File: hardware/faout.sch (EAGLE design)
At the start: 159 parts, among them IC2 MT48LC8M16A2, P1 TE_CONN_MTE_HEADER3R, Q1 L7812ACV, Q2 L7912ACV, Q3 12MHz, Q4 ASFL, U1 LM3671MF-3.3, U10 REF102AU, U11 OPA4277UA, U12 DAC8812, U13 REF102AU, U14 OPA4277UA, U15 DAC8812, U2 LM3671MF-1.2, U3 93LC46BT-I/OT, U4 6SLX9TQG144, U5 M25PE16SO8N, U6 OPA2277UA/2K5E4, U7 REF102AU, U8 OPA4277UA, U9 DAC8812

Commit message: Order code corrections and additions.
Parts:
- C17, C9: OC_FARNELL 9693467 -> 317287
- R18, R19, R22, R23, R24, R25, R28, R29, R30, R31, R34, R35: OC_FARNELL (none) -> 1688472

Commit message: Update UCF file for new board layout.
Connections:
- removed net P1_8: SV2.8, U4B1.IO_L32N_1
- new net P1_0: SV2.1, U4B1.IO_L42P_GCLK7_1
- net P1_1: now also SV2.2, U4B1.IO_L42N_GCLK6_TRDY1_1; no longer SV2.1, U4B1.IO_L42P_GCLK7_1
- net P1_2: now also SV2.3, U4B1.IO_L41P_GCLK9_IRDY1_1; no longer SV2.2, U4B1.IO_L42N_GCLK6_TRDY1_1
- net P1_3: now also SV2.4, U4B1.IO_L41N_GCLK8_1; no longer SV2.3, U4B1.IO_L41P_GCLK9_IRDY1_1
- net P1_4: now also SV2.5, U4B1.IO_L33P_1; no longer SV2.4, U4B1.IO_L41N_GCLK8_1
- net P1_5: now also SV2.6, U4B1.IO_L33N_1; no longer SV2.5, U4B1.IO_L33P_1
- net P1_6: now also SV2.7, U4B1.IO_L32P_1; no longer SV2.6, U4B1.IO_L33N_1
- net P1_7: now also SV2.8, U4B1.IO_L32N_1; no longer SV2.7, U4B1.IO_L32P_1
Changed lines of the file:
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@@
 </segment>
 <segment>
-<wire x1="248.92" y1="-116.84" x2="236.22" y2="-116.84" width="0.1524" layer="91"/>
+<wire x1="248.92" y1="-116.84" x2="233.68" y2="-116.84" width="0.1524" layer="91"/>
 <label x="236.22" y="-116.84" size="1.778" layer="95"/>
 <pinref part="U4" gate="B0" pin="IO_L3P_0"/>
-<junction x="236.22" y="-116.84"/>
-<wire x1="236.22" y1="-116.84" x2="233.68" y2="-116.84" width="0.1524" layer="91"/>
 </segment>
 </net>
@@
 </segment>
 <segment>
-<wire x1="248.92" y1="-124.46" x2="236.22" y2="-124.46" width="0.1524" layer="91"/>
+<wire x1="248.92" y1="-124.46" x2="233.68" y2="-124.46" width="0.1524" layer="91"/>
 <label x="236.22" y="-124.46" size="1.778" layer="95"/>
 <pinref part="U4" gate="B0" pin="IO_L2N_0"/>
-<junction x="236.22" y="-124.46"/>
-<wire x1="236.22" y1="-124.46" x2="233.68" y2="-124.46" width="0.1524" layer="91"/>
 </segment>
 </net>
@@
 </segment>
 </net>
+<net name="P1_0" class="0">
+<segment>
+<pinref part="U4" gate="B1" pin="IO_L42P_GCLK7_1"/>
+<wire x1="233.68" y1="-198.12" x2="248.92" y2="-198.12" width="0.1524" layer="91"/>
+<label x="236.22" y="-198.12" size="1.778" layer="95"/>
+</segment>
+<segment>
+<wire x1="10.16" y1="-279.4" x2="22.86" y2="-279.4" width="0.1524" layer="91"/>
+<label x="12.7" y="-279.4" size="1.778" layer="95"/>
+<pinref part="SV2" gate="G$1" pin="1"/>
+</segment>
+</net>
+<net name="P1_3" class="0">
+<segment>
+<pinref part="U4" gate="B1" pin="IO_L41N_GCLK8_1"/>
+<wire x1="233.68" y1="-190.5" x2="248.92" y2="-190.5" width="0.1524" layer="91"/>
+<label x="236.22" y="-190.5" size="1.778" layer="95"/>
+</segment>
+<segment>
+<wire x1="-17.78" y1="-276.86" x2="-5.08" y2="-276.86" width="0.1524" layer="91"/>
+<label x="-15.24" y="-276.86" size="1.778" layer="95"/>
+<pinref part="SV2" gate="G$1" pin="4"/>
+</segment>
+</net>
 <net name="P1_2" class="0">
+<segment>
+<pinref part="U4" gate="B1" pin="IO_L41P_GCLK9_IRDY1_1"/>
+<wire x1="233.68" y1="-193.04" x2="248.92" y2="-193.04" width="0.1524" layer="91"/>
+<label x="236.22" y="-193.04" size="1.778" layer="95"/>
+</segment>
+<segment>
+<wire x1="10.16" y1="-276.86" x2="22.86" y2="-276.86" width="0.1524" layer="91"/>
+<label x="12.7" y="-276.86" size="1.778" layer="95"/>
+<pinref part="SV2" gate="G$1" pin="3"/>
+</segment>
+</net>
+<net name="P1_6" class="0">
+<segment>
+<pinref part="U4" gate="B1" pin="IO_L32P_1"/>
+<wire x1="233.68" y1="-172.72" x2="248.92" y2="-172.72" width="0.1524" layer="91"/>
+<label x="236.22" y="-172.72" size="1.778" layer="95"/>
+</segment>
+<segment>
+<wire x1="10.16" y1="-271.78" x2="22.86" y2="-271.78" width="0.1524" layer="91"/>
+<label x="12.7" y="-271.78" size="1.778" layer="95"/>
+<pinref part="SV2" gate="G$1" pin="7"/>
+</segment>
+</net>
+<net name="P1_7" class="0">
+<segment>
+<pinref part="U4" gate="B1" pin="IO_L32N_1"/>
+<wire x1="233.68" y1="-170.18" x2="248.92" y2="-170.18" width="0.1524" layer="91"/>
+<label x="236.22" y="-170.18" size="1.778" layer="95"/>
+</segment>
+<segment>
+<wire x1="-17.78" y1="-271.78" x2="-5.08" y2="-271.78" width="0.1524" layer="91"/>
+<label x="-15.24" y="-271.78" size="1.778" layer="95"/>
+<pinref part="SV2" gate="G$1" pin="8"/>
+</segment>
+</net>
+<net name="P1_4" class="0">
+<segment>
+<pinref part="U4" gate="B1" pin="IO_L33P_1"/>
+<wire x1="248.92" y1="-177.8" x2="233.68" y2="-177.8" width="0.1524" layer="91"/>
+<label x="236.22" y="-177.8" size="1.778" layer="95"/>
+</segment>
+<segment>
+<wire x1="22.86" y1="-274.32" x2="10.16" y2="-274.32" width="0.1524" layer="91"/>
+<label x="12.7" y="-274.32" size="1.778" layer="95"/>
+<pinref part="SV2" gate="G$1" pin="5"/>
+</segment>
+</net>
+<net name="P1_5" class="0">
+<segment>
+<pinref part="U4" gate="B1" pin="IO_L33N_1"/>
+<wire x1="233.68" y1="-175.26" x2="248.92" y2="-175.26" width="0.1524" layer="91"/>
+<label x="236.22" y="-175.26" size="1.778" layer="95"/>
+</segment>
+<segment>
+<wire x1="-17.78" y1="-274.32" x2="-5.08" y2="-274.32" width="0.1524" layer="91"/>
+<label x="-15.24" y="-274.32" size="1.778" layer="95"/>
+<pinref part="SV2" gate="G$1" pin="6"/>
+</segment>
+</net>
+<net name="P1_1" class="0">
+<segment>
+<wire x1="-17.78" y1="-279.4" x2="-5.08" y2="-279.4" width="0.1524" layer="91"/>
+<label x="-15.24" y="-279.4" size="1.778" layer="95"/>
+<pinref part="SV2" gate="G$1" pin="2"/>
+</segment>
 <segment>
 <pinref part="U4" gate="B1" pin="IO_L42N_GCLK6_TRDY1_1"/>
@@
 <label x="236.22" y="-195.58" size="1.778" layer="95"/>
 </segment>
-<segment>
-<wire x1="-17.78" y1="-279.4" x2="-5.08" y2="-279.4" width="0.1524" layer="91"/>
-<label x="-15.24" y="-279.4" size="1.778" layer="95"/>
-<pinref part="SV2" gate="G$1" pin="2"/>
-</segment>
-</net>
-<net name="P1_1" class="0">
-<segment>
-<pinref part="U4" gate="B1" pin="IO_L42P_GCLK7_1"/>
-<wire x1="233.68" y1="-198.12" x2="248.92" y2="-198.12" width="0.1524" layer="91"/>
-<label x="236.22" y="-198.12" size="1.778" layer="95"/>
-</segment>
-<segment>
-<wire x1="10.16" y1="-279.4" x2="22.86" y2="-279.4" width="0.1524" layer="91"/>
-<label x="12.7" y="-279.4" size="1.778" layer="95"/>
-<pinref part="SV2" gate="G$1" pin="1"/>
-</segment>
-</net>
-<net name="P1_4" class="0">
-<segment>
-<pinref part="U4" gate="B1" pin="IO_L41N_GCLK8_1"/>
-<wire x1="233.68" y1="-190.5" x2="248.92" y2="-190.5" width="0.1524" layer="91"/>
-<label x="236.22" y="-190.5" size="1.778" layer="95"/>
-</segment>
-<segment>
-<wire x1="-17.78" y1="-276.86" x2="-5.08" y2="-276.86" width="0.1524" layer="91"/>
-<label x="-15.24" y="-276.86" size="1.778" layer="95"/>
-<pinref part="SV2" gate="G$1" pin="4"/>
-</segment>
-</net>
-<net name="P1_3" class="0">
-<segment>
-<pinref part="U4" gate="B1" pin="IO_L41P_GCLK9_IRDY1_1"/>
-<wire x1="233.68" y1="-193.04" x2="248.92" y2="-193.04" width="0.1524" layer="91"/>
-<label x="236.22" y="-193.04" size="1.778" layer="95"/>
-</segment>
-<segment>
-<wire x1="10.16" y1="-276.86" x2="22.86" y2="-276.86" width="0.1524" layer="91"/>
-<label x="12.7" y="-276.86" size="1.778" layer="95"/>
-<pinref part="SV2" gate="G$1" pin="3"/>
-</segment>
-</net>
-<net name="P1_7" class="0">
-<segment>
-<pinref part="U4" gate="B1" pin="IO_L32P_1"/>
-<wire x1="233.68" y1="-172.72" x2="248.92" y2="-172.72" width="0.1524" layer="91"/>
-<label x="236.22" y="-172.72" size="1.778" layer="95"/>
-</segment>
-<segment>
-<wire x1="10.16" y1="-271.78" x2="22.86" y2="-271.78" width="0.1524" layer="91"/>
-<label x="12.7" y="-271.78" size="1.778" layer="95"/>
-<pinref part="SV2" gate="G$1" pin="7"/>
-</segment>
-</net>
-<net name="P1_8" class="0">
-<segment>
-<pinref part="U4" gate="B1" pin="IO_L32N_1"/>
-<wire x1="233.68" y1="-170.18" x2="248.92" y2="-170.18" width="0.1524" layer="91"/>
-<label x="236.22" y="-170.18" size="1.778" layer="95"/>
-</segment>
-<segment>
-<wire x1="-17.78" y1="-271.78" x2="-5.08" y2="-271.78" width="0.1524" layer="91"/>
-<label x="-15.24" y="-271.78" size="1.778" layer="95"/>
-<pinref part="SV2" gate="G$1" pin="8"/>
-</segment>
-</net>
-<net name="P1_5" class="0">
-<segment>
-<pinref part="U4" gate="B1" pin="IO_L33P_1"/>
-<wire x1="248.92" y1="-177.8" x2="233.68" y2="-177.8" width="0.1524" layer="91"/>
-<label x="236.22" y="-177.8" size="1.778" layer="95"/>
-</segment>
-<segment>
-<wire x1="22.86" y1="-274.32" x2="10.16" y2="-274.32" width="0.1524" layer="91"/>
-<label x="12.7" y="-274.32" size="1.778" layer="95"/>
-<pinref part="SV2" gate="G$1" pin="5"/>
-</segment>
-</net>
-<net name="P1_6" class="0">
-<segment>
-<pinref part="U4" gate="B1" pin="IO_L33N_1"/>
-<wire x1="233.68" y1="-175.26" x2="248.92" y2="-175.26" width="0.1524" layer="91"/>
-<label x="236.22" y="-175.26" size="1.778" layer="95"/>
-</segment>
-<segment>
-<wire x1="-17.78" y1="-274.32" x2="-5.08" y2="-274.32" width="0.1524" layer="91"/>
-<label x="-15.24" y="-274.32" size="1.778" layer="95"/>
-<pinref part="SV2" gate="G$1" pin="6"/>
-</segment>
-</net>
+</net>

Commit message: Rework DAC power supply. Precision resistor arrays for outputs.
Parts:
- removed R18, R19, R22, R23, R24, R25, R28, R29, R30, R31, R34, R35: 10k, faout:R_EU0603
- removed R20, R21, R26, R27, R32, R33: 5k, faout:R_EU0603
- removed U6: OPA2277UA/2K5E4, faout:OPA2277UA/2K5E4
- added C100, C101, C102, C103, C98, C99: 10uF, faout:C_EU0805
- added C92, C93, C94, C97: 1uF, faout:C_EU0603
- added C95: 220uF, rcl:CPOL-EUE
- added C96: 10nF, faout:C_EU0603
- added RN1, RN2, RN3, RN4, RN5, RN6: 10k, resistor-dil:4R-NEXBV8V
- added U16: LM7321MF, faout:LM7321MF
- C17, C9: value 100uF -> 220uF; OC_FARNELL 317287 -> 9695680
- C73, C82, C91: value 100nF -> 10nF; OC_FARNELL 1740621 -> 1759102
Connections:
- removed net N$20: R27.P$2, R28.P$1, R29.P$2, U11.-IN_C
- removed net N$21: R24.P$1, R25.P$2, R26.P$2, U11.-IN_D
- new net N$16: RN1A.2, RN1B.2, RN1C.2, RN1D.1, U8.-IN_D
- new net N$17: RN3A.2, RN3B.2, RN3C.2, RN3D.1, U11.-IN_D
- net A+12V: now also C100.P$1, C102.P$1, C96.P$1, C97.P$1, C98.P$1, U16.V+; no longer U6.V+
- net A+3V3: now also C92.P$1, C93.P$1, C94.P$1, C95.+, U16.-IN, U16.OUT; no longer U6.-IN_A, U6.OUT_A
- net A-12V: now also C101.P$2, C103.P$2, C99.P$2
- net AGND: now also C100.P$2, C101.P$1, C102.P$2, C103.P$1, C92.P$2, C93.P$2, C94.P$2, C95.-, C96.P$2, C97.P$2, C98.P$2, C99.P$1, U16.V-; no longer U6.V-
- net DAC1_RFBA: now also RN2B.2, RN2C.2; no longer R21.P$1
- net DAC1_RFBB: now also RN1B.1, RN1C.1; no longer R20.P$1
- net DAC1_VOUTA: now also RN2D.1; no longer R23.P$1
- net DAC1_VOUTB: now also RN1D.2; no longer R19.P$1
- net DAC1_VREF: now also RN1A.1, RN2A.2; no longer R18.P$2, R22.P$2
- net DAC2_RFBA: now also RN4B.2, RN4C.2; no longer R27.P$1
- net DAC2_RFBB: now also RN3B.1, RN3C.1; no longer R26.P$1
- net DAC2_VOUTA: now also RN4D.1; no longer R29.P$1
- net DAC2_VOUTB: now also RN3D.2; no longer R25.P$1
- net DAC2_VREF: now also RN3A.1, RN4A.2; no longer R24.P$2, R28.P$2
- net DAC3_RFBA: now also RN6B.2, RN6C.2; no longer R33.P$1
- net DAC3_RFBB: now also RN5B.1, RN5C.1; no longer R32.P$1
- net DAC3_VOUTA: now also RN6D.1; no longer R35.P$1
- net DAC3_VOUTB: now also RN5D.2; no longer R31.P$1
- net DAC3_VREF: now also RN5A.1, RN6A.2; no longer R30.P$2, R34.P$2
- net N$10: now also RN5A.2, RN5B.2, RN5C.2, RN5D.1; no longer R30.P$1, R31.P$2, R32.P$2
- net N$13: now also U16.+IN; no longer U6.+IN_A
- net N$14: now also RN6A.1, RN6B.1, RN6C.1, RN6D.2; no longer R33.P$2, R34.P$1, R35.P$2
- net N$8: now also RN2A.1, RN2B.1, RN2C.1, RN2D.2; no longer R21.P$2, R22.P$1, R23.P$2
- net N$9: now also RN4A.1, RN4B.1, RN4C.1, RN4D.2, U11.-IN_C; no longer R18.P$1, R19.P$2, R20.P$2, U8.-IN_D
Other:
- moved on the sheet: C73, C82, C91, R16, R17

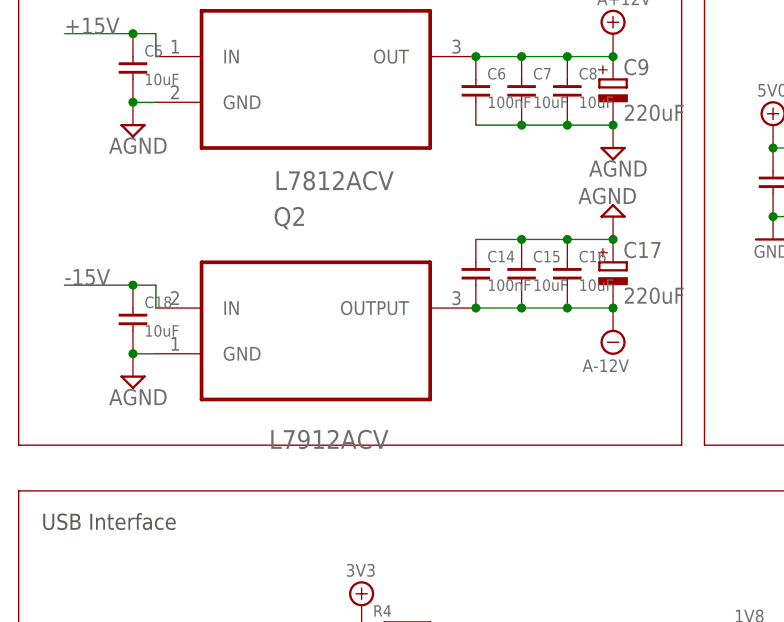
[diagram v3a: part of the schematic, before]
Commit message: Analog power supply with low profile components.
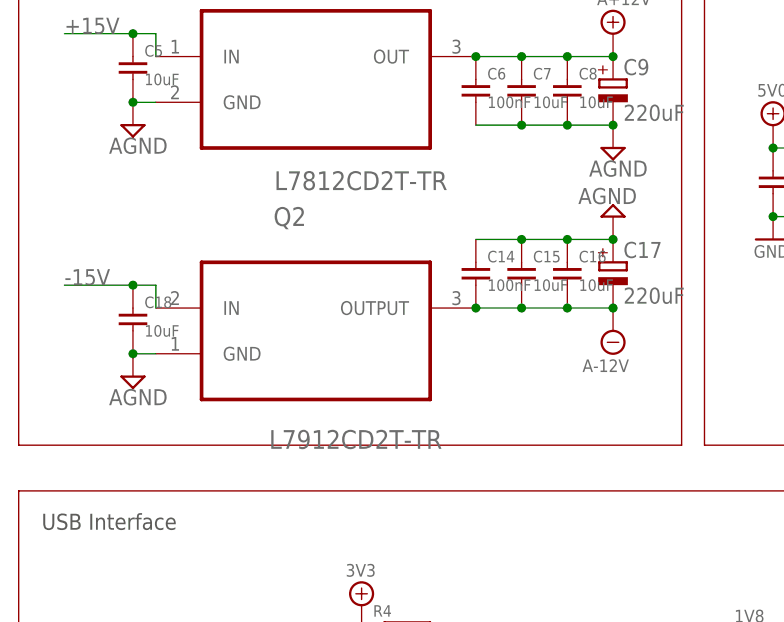
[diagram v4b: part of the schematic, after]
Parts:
- Q1: value L7812ACV -> L7812CD2T-TR; device faout:L7812ACV -> faout:L7812CD2T-TR
- Q2: value L7912ACV -> L7912CD2T-TR; device faout:L7912ACV -> faout:L7912CD2T-TR
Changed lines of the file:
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@@
 <attribute name="OC_FARNELL" value="1833803"/>
 </part>
-<part name="Q1" library="faout" deviceset="L7812ACV" device=""/>
-<part name="Q2" library="faout" deviceset="L7912ACV" device=""/>
+<part name="Q1" library="faout" deviceset="L7812CD2T-TR" device=""/>
+<part name="Q2" library="faout" deviceset="L7912CD2T-TR" device=""/>
 <part name="A+12V_PWR1" library="faout" deviceset="A+12V" device=""/>
 <part name="A-12V_PWR1" library="faout" deviceset="A-12V" device=""/>

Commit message: Add and correct Farnell order codes.
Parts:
- Q1: OC_FARNELL (none) -> 2296017
- R1, R3: OC_FARNELL (none) -> 1612060
- R4, R5: OC_FARNELL (none) -> 1463451
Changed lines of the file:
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@@
 <part name="GND_PWR10" library="faout" deviceset="GND" device=""/>
 <part name="GND_PWR9" library="faout" deviceset="GND" device=""/>
-<part name="R4" library="faout" deviceset="R_EU" device="0603" value="ferrite"/>
-<part name="R5" library="faout" deviceset="R_EU" device="0603" value="ferrite"/>
+<part name="R4" library="faout" deviceset="R_EU" device="0603" value="ferrite">
+<attribute name="OC_FARNELL" value="1463451"/>
+</part>
+<part name="R5" library="faout" deviceset="R_EU" device="0603" value="ferrite">
+<attribute name="OC_FARNELL" value="1463451"/>
+</part>
 <part name="C19" library="faout" deviceset="C_EU" device="0603" value="4.7uF">
 <attribute name="OC_FARNELL" value="1833803"/>
@@
 <attribute name="OC_FARNELL" value="1833803"/>
 </part>
-<part name="Q1" library="faout" deviceset="L7812CD2T-TR" device=""/>
+<part name="Q1" library="faout" deviceset="L7812CD2T-TR" device="">
+<attribute name="OC_FARNELL" value="2296017"/>
+</part>
 <part name="Q2" library="faout" deviceset="L7912CD2T-TR" device=""/>
 <part name="A+12V_PWR1" library="faout" deviceset="A+12V" device=""/>
@@
 <part name="GND_PWR21" library="faout" deviceset="GND" device=""/>
 <part name="R7" library="faout" deviceset="R_EU" device="0603" value="NC"/>
-<part name="R1" library="faout" deviceset="R_EU" device="1206" value="ferrite"/>
-<part name="R3" library="faout" deviceset="R_EU" device="1206" value="ferrite"/>
+<part name="R1" library="faout" deviceset="R_EU" device="1206" value="ferrite">
+<attribute name="OC_FARNELL" value="1612060"/>
+</part>
+<part name="R3" library="faout" deviceset="R_EU" device="1206" value="ferrite">
+<attribute name="OC_FARNELL" value="1612060"/>
+</part>
 <part name="5V0_PWR1" library="Bogdan_Commons" deviceset="5V0" device=""/>
 <part name="GND_PWR2" library="Bogdan_Commons" deviceset="GND" device=""/>
@@
 <instance part="GND_PWR10" gate="A" x="45.72" y="-60.96"/>
 <instance part="GND_PWR9" gate="A" x="40.64" y="-60.96"/>
-<instance part="R4" gate="G$1" x="20.32" y="-45.72"/>
-<instance part="R5" gate="G$1" x="20.32" y="-48.26"/>
+<instance part="R4" gate="G$1" x="20.32" y="-45.72">
+<attribute name="OC_FARNELL" x="20.32" y="-45.72" size="1.778" layer="96" display="off"/>
+</instance>
+<instance part="R5" gate="G$1" x="20.32" y="-48.26">
+<attribute name="OC_FARNELL" x="20.32" y="-48.26" size="1.778" layer="96" display="off"/>
+</instance>
 <instance part="C19" gate="G$1" x="27.94" y="-53.34">
 <attribute name="OC_FARNELL" x="27.94" y="-53.34" size="1.778" layer="96" display="off"/>
@@
 <instance part="GND_PWR21" gate="A" x="-5.08" y="-236.22" rot="R180"/>
 <instance part="R7" gate="G$1" x="53.34" y="-142.24" rot="R270"/>
-<instance part="R1" gate="G$1" x="116.84" y="63.5"/>
-<instance part="R3" gate="G$1" x="116.84" y="58.42"/>
+<instance part="R1" gate="G$1" x="116.84" y="63.5">
+<attribute name="OC_FARNELL" x="116.84" y="63.5" size="1.778" layer="96" display="off"/>
+</instance>
+<instance part="R3" gate="G$1" x="116.84" y="58.42">
+<attribute name="OC_FARNELL" x="116.84" y="58.42" size="1.778" layer="96" display="off"/>
+</instance>
 <instance part="5V0_PWR1" gate="A" x="127" y="66.04"/>
 <instance part="GND_PWR2" gate="A" x="127" y="55.88"/>

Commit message: Replace USB connector. Minor changes for production.
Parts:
- C31: value 3.3uF -> 4.7uF
- R14: value 4.7k -> 10k
- R16: value 13.181k -> 13k
- R17: value 5k -> 5.1k
- R2: OC_FARNELL (none) -> 1612060
- USB1: value (none) -> MOLEX_USB_105017-0001; device molex_usb:47346-0001 -> faout:MOLEX_USB_105017-0001
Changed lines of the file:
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@@
 <part name="GND_PWR12" library="faout" deviceset="GND" device=""/>
 <part name="1V8_PWR3" library="faout" deviceset="1V8" device=""/>
-<part name="C31" library="faout" deviceset="C_EU" device="0603" value="3.3uF">
+<part name="C31" library="faout" deviceset="C_EU" device="0603" value="4.7uF">
 <attribute name="OC_FARNELL" value="1833803"/>
 </part>
@@
 <part name="GND_PWR33" library="faout" deviceset="GND" device=""/>
 <part name="GND_PWR41" library="faout" deviceset="GND" device=""/>
-<part name="R14" library="faout" deviceset="R_EU" device="0603" value="4.7k"/>
+<part name="R14" library="faout" deviceset="R_EU" device="0603" value="10k"/>
 <part name="3V3_PWR27" library="faout" deviceset="3V3" device=""/>
 <part name="Q4" library="crystal" deviceset="ASF*" device="" technology="L"/>
@@
 <part name="AO6" library="analog_out_lib" deviceset="BU-SMA" device=""/>
 <part name="SUPPLY43" library="supply2" deviceset="AGND" device=""/>
-<part name="USB1" library="molex_usb" deviceset="47346-0001" device=""/>
 <part name="R9" library="faout" deviceset="R_EU" device="0603"/>
 <part name="SUPPLY17" library="supply2" deviceset="AGND" device=""/>
@@
 <part name="A+3V3_PWR6" library="faout" deviceset="A+3V3" device=""/>
 <part name="A+3V3_PWR9" library="faout" deviceset="A+3V3" device=""/>
-<part name="R16" library="faout" deviceset="R_EU" device="0603" value="13.181k"/>
-<part name="R17" library="faout" deviceset="R_EU" device="0603" value="5k"/>
+<part name="R16" library="faout" deviceset="R_EU" device="0603" value="13k"/>
+<part name="R17" library="faout" deviceset="R_EU" device="0603" value="5.1k"/>
 <part name="A+12V_PWR2" library="faout" deviceset="A+12V" device=""/>
 <part name="SUPPLY8" library="supply2" deviceset="AGND" device=""/>
@@
 <part name="GND_PWR1" library="Bogdan_Commons" deviceset="GND" device=""/>
 <part name="SUPPLY1" library="supply2" deviceset="AGND" device=""/>
-<part name="R2" library="faout" deviceset="R_EU" device="1206" value="ferrite"/>
+<part name="R2" library="faout" deviceset="R_EU" device="1206" value="ferrite">
+<attribute name="OC_FARNELL" value="1612060"/>
+</part>
 <part name="GND_PWR42" library="faout" deviceset="GND" device=""/>
 <part name="GND_PWR40" library="faout" deviceset="GND" device=""/>
@@
 <attribute name="OC_FARNELL" value="1735530"/>
 </part>
+<part name="USB1" library="faout" deviceset="MOLEX_USB_" device="105017-0001"/>
 </parts>
 <sheets>
@@
 <instance part="AO6" gate="G$1" x="429.26" y="-243.84" rot="MR0"/>
 <instance part="SUPPLY43" gate="G$1" x="426.72" y="-264.16"/>
-<instance part="USB1" gate="G$1" x="-7.62" y="-127" rot="MR0"/>
 <instance part="R9" gate="G$1" x="-5.08" y="-152.4"/>
 <instance part="SUPPLY17" gate="G$1" x="373.38" y="-33.02" rot="R270"/>
@@
 <instance part="GND_PWR1" gate="A" x="60.96" y="58.42"/>
 <instance part="SUPPLY1" gate="G$1" x="40.64" y="58.42"/>
-<instance part="R2" gate="G$1" x="50.8" y="60.96"/>
+<instance part="R2" gate="G$1" x="50.8" y="60.96">
+<attribute name="OC_FARNELL" x="50.8" y="60.96" size="1.778" layer="96" display="off"/>
+</instance>
 <instance part="GND_PWR42" gate="A" x="251.46" y="-182.88" rot="R90"/>
 <instance part="GND_PWR40" gate="A" x="251.46" y="-180.34" rot="R90"/>
@@
 <attribute name="OC_FARNELL" x="396.24" y="-210.82" size="1.778" layer="96" rot="R90" display="off"/>
 </instance>
+<instance part="USB1" gate="G$1" x="-7.62" y="-127" rot="MR0"/>
 </instances>
 <busses>
@@
 <net name="USB_GND" class="0">
 <segment>
-<pinref part="USB1" gate="G$1" pin="GND"/>
 <wire x1="2.54" y1="-132.08" x2="17.78" y2="-132.08" width="0.1524" layer="91"/>
 <label x="5.08" y="-132.08" size="1.778" layer="95"/>
@@
 <pinref part="R9" gate="G$1" pin="P$2"/>
 <wire x1="2.54" y1="-152.4" x2="0" y2="-152.4" width="0.1524" layer="91"/>
+<pinref part="USB1" gate="G$1" pin="GND"/>
 <junction x="2.54" y="-132.08"/>
 </segment>
@@
 <net name="USB_V" class="0">
 <segment>
-<pinref part="USB1" gate="G$1" pin="V_BUS"/>
 <wire x1="2.54" y1="-121.92" x2="17.78" y2="-121.92" width="0.1524" layer="91"/>
 <label x="5.08" y="-121.92" size="1.778" layer="95"/>
+<pinref part="USB1" gate="G$1" pin="V_BUS"/>
 </segment>
 <segment>
@@
 <net name="N$15" class="0">
 <segment>
-<pinref part="USB1" gate="G$1" pin="SHD@4"/>
 <wire x1="-12.7" y1="-148.59" x2="-12.7" y2="-152.4" width="0.1524" layer="91"/>
 <wire x1="-12.7" y1="-152.4" x2="-10.16" y2="-152.4" width="0.1524" layer="91"/>
 <pinref part="R9" gate="G$1" pin="P$1"/>
+<pinref part="USB1" gate="G$1" pin="SHD@4"/>
 </segment>
 </net>
